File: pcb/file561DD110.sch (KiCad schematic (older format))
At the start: 25 parts

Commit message: starting on layout
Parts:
- C21, C22: renamed from C?; footprint (none) -> Capacitors_SMD:C_0805_HandSoldering
- D10, D9: renamed from D?; footprint (none) -> LEDs:LED-0805
- P12: renamed from P?; footprint (none) -> Pin_Headers:Pin_Header_Straight_1x02
- Q18, Q20: renamed from Q?; footprint SOT-23 -> Housings_SOT-23_SOT-143_TSOT-6:SOT-23_Handsoldering
- Q19, Q21: renamed from Q?; footprint TO-220 -> Power_Integrations:TO-220
- R67, R68, R69, R70, R71, R74, R80, R81: renamed from R?; footprint (none) -> Resistors_ThroughHole:Resistor_Horizontal_RM10mm
- R72, R73, R75, R76, R77, R78: renamed from R?; footprint (none) -> Resistors_SMD:R_0805_HandSoldering
- R79: renamed from R?; value R -> 0R056; footprint (none) -> Resistors_SMD:R_2512_HandSoldering; symbol R-RESCUE-BatAger -> R; Part # (none) -> RL2512 FK-07 0R056
- U6: renamed from U?; footprint (none) -> Housings_SOIC:SOIC-8_3.9x4.9mm_Pitch1.27mm

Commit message: trace complete (maybe!)
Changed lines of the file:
@@
 	4350 2550 4350 2600
 Wire Wire Line
-	4000 1800 4550 1800
+	4000 1800 4650 1800
 Wire Wire Line
 	4350 1800 4350 2150
@@
 shunt5_high
 Wire Wire Line
-	5050 1800 5350 1800
+	4950 1800 5350 1800
 Wire Wire Line
 	5100 1800 5100 1600

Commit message: adding planes - almost done!
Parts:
- added P16: FAN, Pin_Headers:Pin_Header_Straight_1x02, symbol CONN_01X02
- added Q22: CSD18536KCS, Power_Integrations:TO-220, symbol Q_NMOS_GDS
- added R82: 220, Resistors_SMD:R_0805_HandSoldering, symbol R
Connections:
- net +15V: now also P16.1 (P1)
- net GND: now also Q22.3 (S)
- new net: P16.2 (P2), Q22.2 (D)
- new net: Q22.1 (G), R82.1
- new net fan_ctrl: R82.2
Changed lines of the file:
@@
 Text Label 2700 5750 0    80   ~ 0
 bat5+
+$Comp
+L CONN_01X02 P16
+U 1 1 561F6C0F
+P 9350 2950
+F 0 "P16" H 9350 3100 50  0000 C CNN
+F 1 "FAN" V 9450 2950 50  0000 C CNN
+F 2 "Pin_Headers:Pin_Header_Straight_1x02" H 9350 2950 60  0001 C CNN
+F 3 "" H 9350 2950 60  0000 C CNN
+	1    9350 2950
+	1    0    0    -1
+$EndComp
+$Comp
+L Q_NMOS_GDS Q22
+U 1 1 561F6CDD
+P 8850 3300
+F 0 "Q22" H 9150 3350 50  0000 R CNN
+F 1 "CSD18536KCS" H 9500 3250 50  0000 R CNN
+F 2 "Power_Integrations:TO-220" H 9050 3400 29  0001 C CNN
+F 3 "" H 8850 3300 60  0000 C CNN
+	1    8850 3300
+	1    0    0    -1
+$EndComp
+Wire Wire Line
+	9150 3000 8950 3000
+Wire Wire Line
+	8950 3000 8950 3100
+$Comp
+L GND #PWR0104
+U 1 1 561F6DC6
+P 8950 3600
+F 0 "#PWR0104" H 8950 3350 50  0001 C CNN
+F 1 "GND" H 8950 3450 50  0000 C CNN
+F 2 "" H 8950 3600 60  0000 C CNN
+F 3 "" H 8950 3600 60  0000 C CNN
+	1    8950 3600
+	1    0    0    -1
+$EndComp
+Wire Wire Line
+	8950 3500 8950 3600
+$Comp
+L R R82
+U 1 1 561F6E96
+P 8400 3300
+F 0 "R82" V 8480 3300 50  0000 C CNN
+F 1 "220" V 8400 3300 50  0000 C CNN
+F 2 "Resistors_SMD:R_0805_HandSoldering" V 8330 3300 30  0001 C CNN
+F 3 "" H 8400 3300 30  0000 C CNN
+	1    8400 3300
+	0    1    1    0
+$EndComp
+Wire Wire Line
+	8650 3300 8550 3300
+Wire Wire Line
+	8250 3300 7950 3300
+Wire Wire Line
+	9150 2900 8800 2900
+Text Label 8800 2900 0    40   ~ 0
++15V
+Text HLabel 7950 3300 0    40   Input ~ 0
+fan_ctrl
 $EndSCHEMATC

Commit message: Production candidate - passes DRC.
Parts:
- R67, R68, R69, R70, R71, R74, R80, R81: footprint Resistors_ThroughHole:Resistor_Horizontal_RM10mm -> Custom Footprints:Resistor_Horizontal_RM10mm
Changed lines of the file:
@@
 F 0 "R81" V 5230 4050 50  0000 C CNN
 F 1 "R" V 5150 4050 50  0000 C CNN
-F 2 "Resistors_ThroughHole:Resistor_Horizontal_RM10mm" V 5080 4050 30  0001 C CNN
+F 2 "Custom Footprints:Resistor_Horizontal_RM10mm" V 5080 4050 30  0001 C CNN
 F 3 "" H 5150 4050 30  0000 C CNN
 	1    5150 4050
@@
 F 0 "R80" V 5230 3500 50  0000 C CNN
 F 1 "R" V 5150 3500 50  0000 C CNN
-F 2 "Resistors_ThroughHole:Resistor_Horizontal_RM10mm" V 5080 3500 30  0001 C CNN
+F 2 "Custom Footprints:Resistor_Horizontal_RM10mm" V 5080 3500 30  0001 C CNN
 F 3 "" H 5150 3500 30  0000 C CNN
 	1    5150 3500
@@
 F 0 "R71" V 1880 3150 50  0000 C CNN
 F 1 "R" V 1800 3150 50  0000 C CNN
-F 2 "Resistors_ThroughHole:Resistor_Horizontal_RM10mm" V 1730 3150 30  0001 C CNN
+F 2 "Custom Footprints:Resistor_Horizontal_RM10mm" V 1730 3150 30  0001 C CNN
 F 3 "" H 1800 3150 30  0000 C CNN
 	1    1800 3150
@@
 F 0 "R67" V 1480 3400 50  0000 C CNN
 F 1 "R" V 1400 3400 50  0000 C CNN
-F 2 "Resistors_ThroughHole:Resistor_Horizontal_RM10mm" V 1330 3400 30  0001 C CNN
+F 2 "Custom Footprints:Resistor_Horizontal_RM10mm" V 1330 3400 30  0001 C CNN
 F 3 "" H 1400 3400 30  0000 C CNN
 	1    1400 3400
@@
 F 0 "R68" V 1680 3550 50  0000 C CNN
 F 1 "R" V 1600 3550 50  0000 C CNN
-F 2 "Resistors_ThroughHole:Resistor_Horizontal_RM10mm" V 1530 3550 30  0001 C CNN
+F 2 "Custom Footprints:Resistor_Horizontal_RM10mm" V 1530 3550 30  0001 C CNN
 F 3 "" H 1600 3550 30  0000 C CNN
 	1    1600 3550
@@
 F 0 "R74" V 3080 3150 50  0000 C CNN
 F 1 "R" V 3000 3150 50  0000 C CNN
-F 2 "Resistors_ThroughHole:Resistor_Horizontal_RM10mm" V 2930 3150 30  0001 C CNN
+F 2 "Custom Footprints:Resistor_Horizontal_RM10mm" V 2930 3150 30  0001 C CNN
 F 3 "" H 3000 3150 30  0000 C CNN
 	1    3000 3150
@@
 F 0 "R69" V 1730 4100 50  0000 C CNN
 F 1 "R" V 1650 4100 50  0000 C CNN
-F 2 "Resistors_ThroughHole:Resistor_Horizontal_RM10mm" V 1580 4100 30  0001 C CNN
+F 2 "Custom Footprints:Resistor_Horizontal_RM10mm" V 1580 4100 30  0001 C CNN
 F 3 "" H 1650 4100 30  0000 C CNN
 	1    1650 4100
@@
 F 0 "R70" V 1730 4600 50  0000 C CNN
 F 1 "R" V 1650 4600 50  0000 C CNN
-F 2 "Resistors_ThroughHole:Resistor_Horizontal_RM10mm" V 1580 4600 30  0001 C CNN
+F 2 "Custom Footprints:Resistor_Horizontal_RM10mm" V 1580 4600 30  0001 C CNN
 F 3 "" H 1650 4600 30  0000 C CNN
 	1    1650 4600

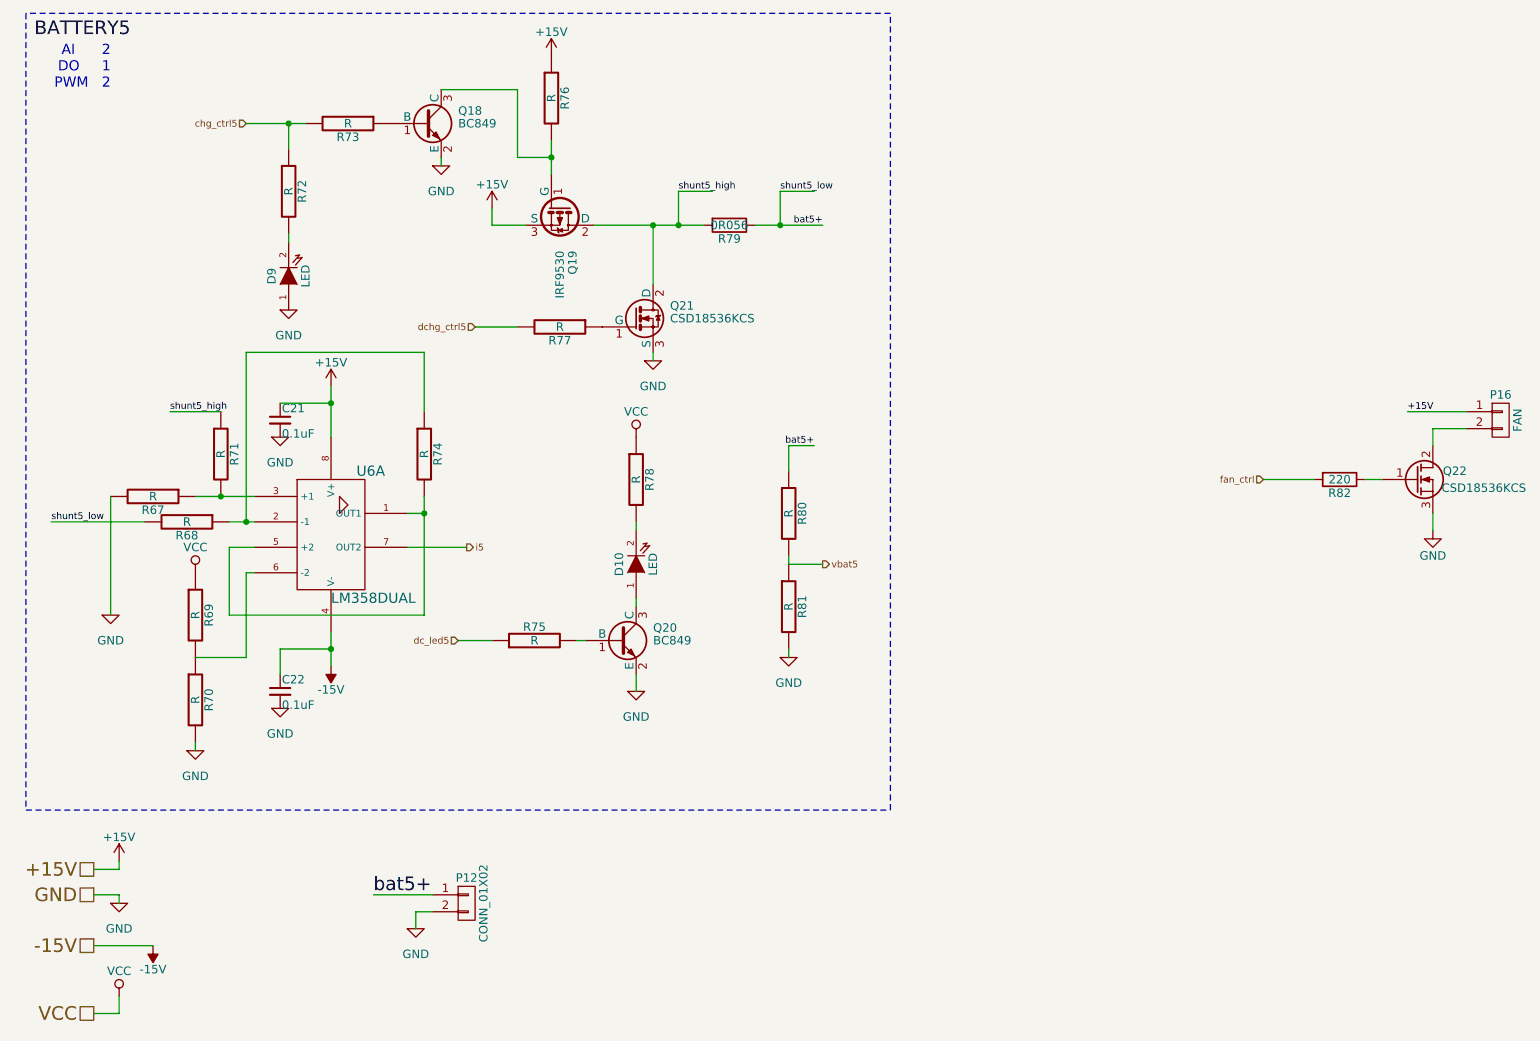
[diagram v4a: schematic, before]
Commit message: Changed fan FET (Q22). Many other minor layout changes. Production candidate.
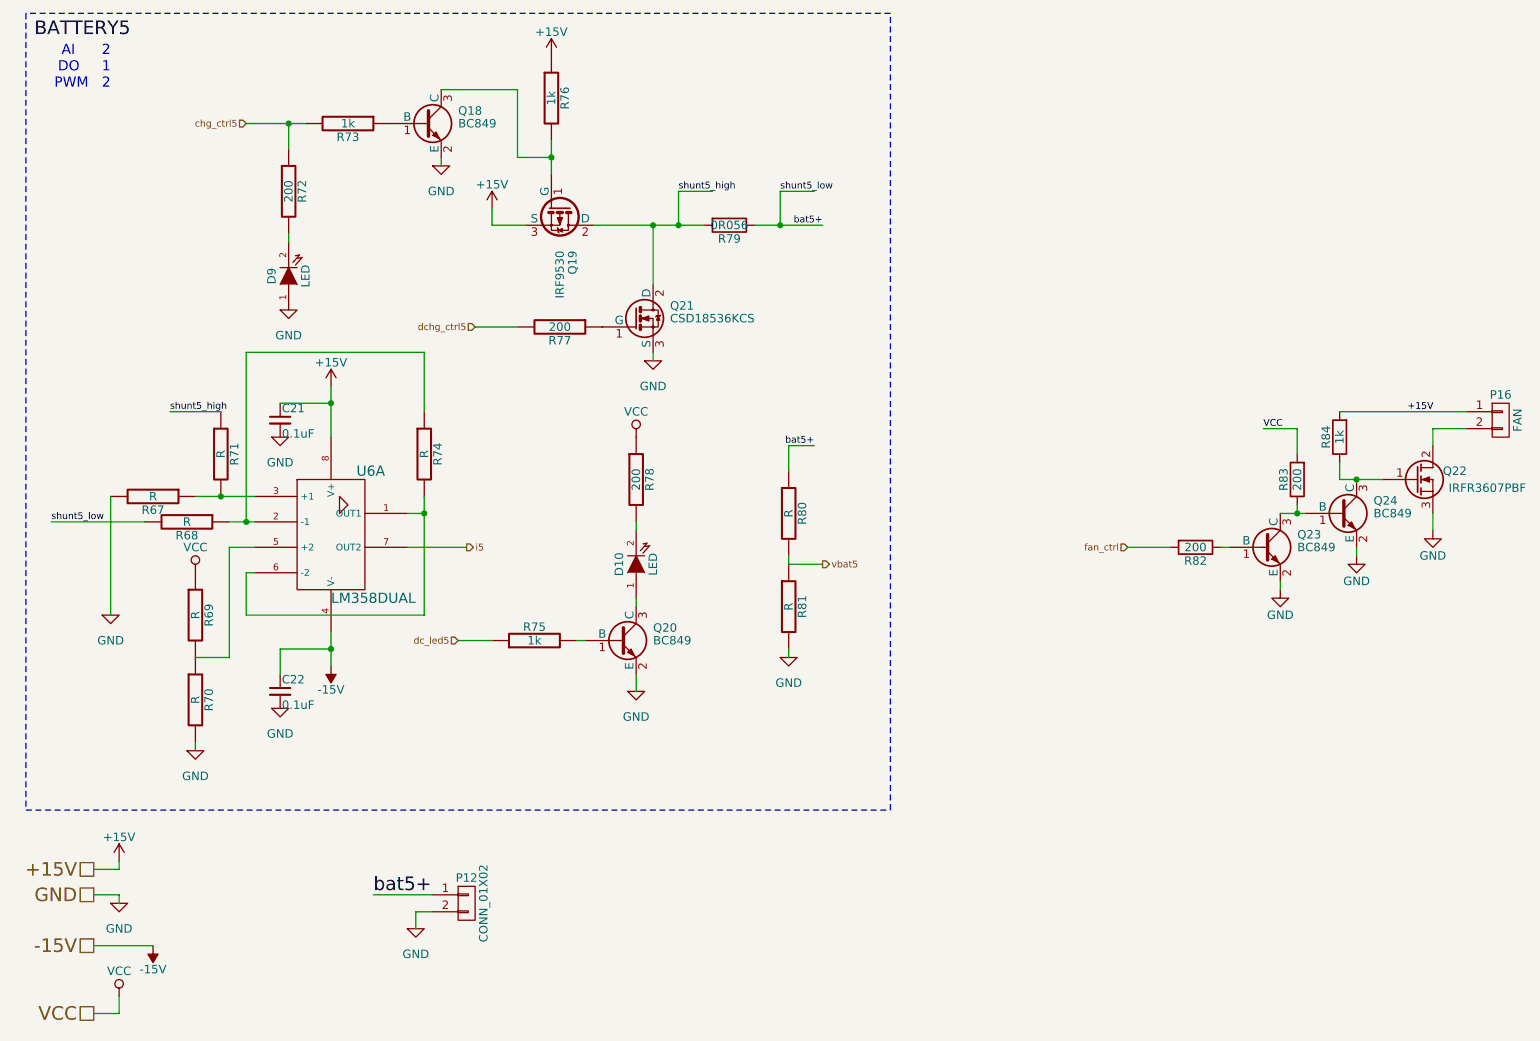
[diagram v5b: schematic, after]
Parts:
- added Q23, Q24: BC849, Housings_SOT-23_SOT-143_TSOT-6:SOT-23_Handsoldering, symbol BC849
- added R83: 200, Resistors_SMD:R_0805_HandSoldering, symbol R
- added R84: 1k, Resistors_SMD:R_0805_HandSoldering, symbol R
- Q19, Q21: footprint Power_Integrations:TO-220 -> Custom Footprints:TO-220
- Q22: value CSD18536KCS -> IRFR3607PBF; footprint Power_Integrations:TO-220 -> TO_SOT_Packages_SMD:TO-252-2Lead
- R72, R77, R78: value R -> 200
- R73, R75, R76: value R -> 1k
- R82: value 220 -> 200
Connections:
- net +15V: now also R84.2
- net GND: now also Q23.2 (E), Q24.2 (E)
- net VCC: now also R83.2
- net at R74.2, U6.1 (OUT1): now also U6.6 (-2); no longer U6.5 (+2)
- net at R69.2, R70.1: now also U6.5 (+2); no longer U6.6 (-2)
- net at Q22.1 (G): now also Q24.3 (C), R84.1; no longer R82.1
- new net: Q23.1 (B), R82.1
- new net: Q23.3 (C), Q24.1 (B), R83.1
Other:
- moved on the sheet: R82
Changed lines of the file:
@@
 F 0 "Q21" H 4450 2425 50  0000 L CNN
 F 1 "CSD18536KCS" H 4450 2350 50  0000 L CNN
-F 2 "Power_Integrations:TO-220" H 4450 2275 50  0001 L CIN
+F 2 "Custom Footprints:TO-220" H 4450 2275 50  0001 L CIN
 F 3 "" H 4250 2350 50  0000 L CNN
 	1    4250 2350
@@
 F 0 "Q19" H 4050 1775 50  0000 L CNN
 F 1 "IRF9530" H 4050 1700 50  0000 L CNN
-F 2 "Power_Integrations:TO-220" H 4050 1625 50  0001 L CIN
+F 2 "Custom Footprints:TO-220" H 4050 1625 50  0001 L CIN
 F 3 "" H 3800 1700 50  0000 L CNN
 	1    3800 1700
@@
 P 4250 3300
 F 0 "R78" V 4330 3300 50  0000 C CNN
-F 1 "R" V 4250 3300 50  0000 C CNN
+F 1 "200" V 4250 3300 50  0000 C CNN
 F 2 "Resistors_SMD:R_0805_HandSoldering" V 4180 3300 30  0001 C CNN
 F 3 "" H 4250 3300 30  0000 C CNN
@@
 P 2200 1600
 F 0 "R72" V 2280 1600 50  0000 C CNN
-F 1 "R" V 2200 1600 50  0000 C CNN
+F 1 "200" V 2200 1600 50  0000 C CNN
 F 2 "Resistors_SMD:R_0805_HandSoldering" V 2130 1600 30  0001 C CNN
 F 3 "" H 2200 1600 30  0000 C CNN
@@
 P 3750 1050
 F 0 "R76" V 3830 1050 50  0000 C CNN
-F 1 "R" V 3750 1050 50  0000 C CNN
+F 1 "1k" V 3750 1050 50  0000 C CNN
 F 2 "Resistors_SMD:R_0805_HandSoldering" V 3680 1050 30  0001 C CNN
 F 3 "" H 3750 1050 30  0000 C CNN
@@
 P 2550 1200
 F 0 "R73" V 2630 1200 50  0000 C CNN
-F 1 "R" V 2550 1200 50  0000 C CNN
+F 1 "1k" V 2550 1200 50  0000 C CNN
 F 2 "Resistors_SMD:R_0805_HandSoldering" V 2480 1200 30  0001 C CNN
 F 3 "" H 2550 1200 30  0000 C CNN
@@
 P 3800 2400
 F 0 "R77" V 3880 2400 50  0000 C CNN
-F 1 "R" V 3800 2400 50  0000 C CNN
+F 1 "200" V 3800 2400 50  0000 C CNN
 F 2 "Resistors_SMD:R_0805_HandSoldering" V 3730 2400 30  0001 C CNN
 F 3 "" H 3800 2400 30  0000 C CNN
@@
 P 3650 4250
 F 0 "R75" V 3730 4250 50  0000 C CNN
-F 1 "R" V 3650 4250 50  0000 C CNN
+F 1 "1k" V 3650 4250 50  0000 C CNN
 F 2 "Resistors_SMD:R_0805_HandSoldering" V 3580 4250 30  0001 C CNN
 F 3 "" H 3650 4250 30  0000 C CNN
@@
 	1350 3550 800  3550
 Wire Wire Line
-	3000 4100 1850 4100
-Wire Wire Line
-	1850 4100 1850 3700
+	1850 3700 1850 4350
 Wire Wire Line
 	1850 3700 2000 3700
@@
 Wire Wire Line
 	2000 3850 1950 3850
-Wire Wire Line
-	1950 3850 1950 4350
-Wire Wire Line
-	1950 4350 1650 4350
 Wire Wire Line
 	1650 4900 1650 4850
@@
 P 8850 3300
 F 0 "Q22" H 9150 3350 50  0000 R CNN
-F 1 "CSD18536KCS" H 9500 3250 50  0000 R CNN
-F 2 "Power_Integrations:TO-220" H 9050 3400 29  0001 C CNN
+F 1 "IRFR3607PBF" H 9500 3250 50  0000 R CNN
+F 2 "TO_SOT_Packages_SMD:TO-252-2Lead" H 9050 3400 29  0001 C CNN
 F 3 "" H 8850 3300 60  0000 C CNN
 	1    8850 3300
@@
 L R R82
 U 1 1 561F6E96
-P 8400 3300
-F 0 "R82" V 8480 3300 50  0000 C CNN
-F 1 "220" V 8400 3300 50  0000 C CNN
-F 2 "Resistors_SMD:R_0805_HandSoldering" V 8330 3300 30  0001 C CNN
-F 3 "" H 8400 3300 30  0000 C CNN
-	1    8400 3300
+P 7550 3700
+F 0 "R82" V 7630 3700 50  0000 C CNN
+F 1 "200" V 7550 3700 50  0000 C CNN
+F 2 "Resistors_SMD:R_0805_HandSoldering" V 7480 3700 30  0001 C CNN
+F 3 "" H 7550 3700 30  0000 C CNN
+	1    7550 3700
 	0    1    1    0
 $EndComp
 Wire Wire Line
-	8650 3300 8550 3300
-Wire Wire Line
-	8250 3300 7950 3300
-Wire Wire Line
-	9150 2900 8800 2900
+	8400 2900 9150 2900
 Text Label 8800 2900 0    40   ~ 0
 +15V
-Text HLabel 7950 3300 0    40   Input ~ 0
+Text HLabel 7150 3700 0    40   Input ~ 0
 fan_ctrl
+Wire Wire Line
+	1850 4350 1650 4350
+Wire Wire Line
+	3000 4100 1950 4100
+Wire Wire Line
+	1950 4100 1950 3850
+$Comp
+L BC849 Q24
+U 1 1 562102C4
+P 8400 3500
+F 0 "Q24" H 8600 3575 50  0000 L CNN
+F 1 "BC849" H 8600 3500 50  0000 L CNN
+F 2 "Housings_SOT-23_SOT-143_TSOT-6:SOT-23_Handsoldering" H 8600 3425 50  0001 L CIN
+F 3 "" H 8400 3500 50  0000 L CNN
+	1    8400 3500
+	1    0    0    -1
+$EndComp
+$Comp
+L R R84
+U 1 1 56210485
+P 8400 3050
+F 0 "R84" V 8480 3050 50  0000 C CNN
+F 1 "1k" V 8400 3050 50  0000 C CNN
+F 2 "Resistors_SMD:R_0805_HandSoldering" V 8330 3050 30  0001 C CNN
+F 3 "" H 8400 3050 30  0000 C CNN
+	1    8400 3050
+	-1   0    0    1
+$EndComp
+$Comp
+L BC849 Q23
+U 1 1 56210668
+P 7950 3700
+F 0 "Q23" H 8150 3775 50  0000 L CNN
+F 1 "BC849" H 8150 3700 50  0000 L CNN
+F 2 "Housings_SOT-23_SOT-143_TSOT-6:SOT-23_Handsoldering" H 8150 3625 50  0001 L CIN
+F 3 "" H 7950 3700 50  0000 L CNN
+	1    7950 3700
+	1    0    0    -1
+$EndComp
+$Comp
+L R R83
+U 1 1 562106DC
+P 8150 3300
+F 0 "R83" V 8230 3300 50  0000 C CNN
+F 1 "200" V 8150 3300 50  0000 C CNN
+F 2 "Resistors_SMD:R_0805_HandSoldering" V 8080 3300 30  0001 C CNN
+F 3 "" H 8150 3300 30  0000 C CNN
+	1    8150 3300
+	-1   0    0    1
+$EndComp
+$Comp
+L GND #PWR0105
+U 1 1 562109D3
+P 8500 3750
+F 0 "#PWR0105" H 8500 3500 50  0001 C CNN
+F 1 "GND" H 8500 3600 50  0000 C CNN
+F 2 "" H 8500 3750 60  0000 C CNN
+F 3 "" H 8500 3750 60  0000 C CNN
+	1    8500 3750
+	1    0    0    -1
+$EndComp
+$Comp
+L GND #PWR0106
+U 1 1 56210A3E
+P 8050 3950
+F 0 "#PWR0106" H 8050 3700 50  0001 C CNN
+F 1 "GND" H 8050 3800 50  0000 C CNN
+F 2 "" H 8050 3950 60  0000 C CNN
+F 3 "" H 8050 3950 60  0000 C CNN
+	1    8050 3950
+	1    0    0    -1
+$EndComp
+Wire Wire Line
+	8400 3300 8650 3300
+Wire Wire Line
+	8400 3300 8400 3200
+Connection ~ 8500 3300
+Wire Wire Line
+	8200 3500 8050 3500
+Wire Wire Line
+	8150 3450 8150 3500
+Connection ~ 8150 3500
+Wire Wire Line
+	7750 3700 7700 3700
+Wire Wire Line
+	8150 3150 8150 3000
+Wire Wire Line
+	8150 3000 7950 3000
+Text Label 7950 3000 0    40   ~ 0
+VCC
+Wire Wire Line
+	7150 3700 7400 3700
+Wire Wire Line
+	8050 3950 8050 3900
+Wire Wire Line
+	8500 3750 8500 3700
 $EndSCHEMATC
